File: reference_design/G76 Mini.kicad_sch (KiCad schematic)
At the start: 28 parts, among them J1 Conn_02x16_Odd_Even, J2 JTAG, J3 DB15_Female_HighDensity, U1 EPM240T100, U2 CY7C1018DV33-10VXI, X1 50MHz

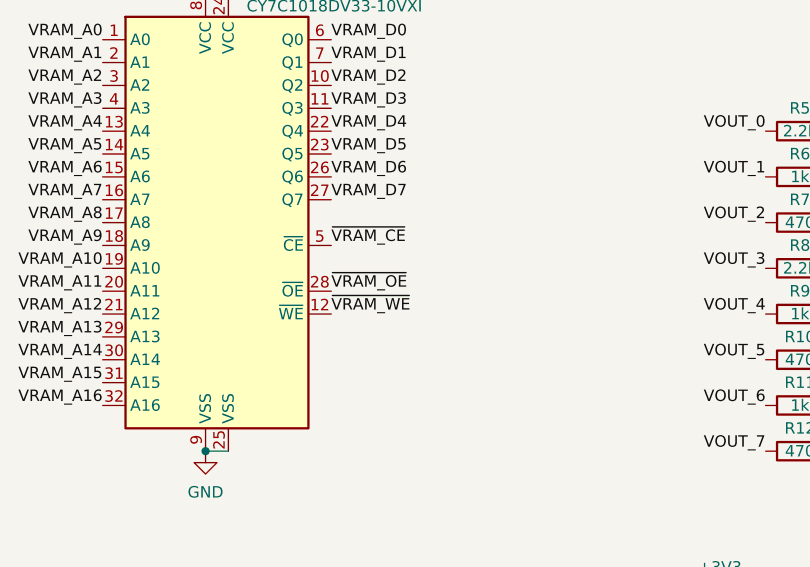
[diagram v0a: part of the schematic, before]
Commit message: Fix CE line on RAM
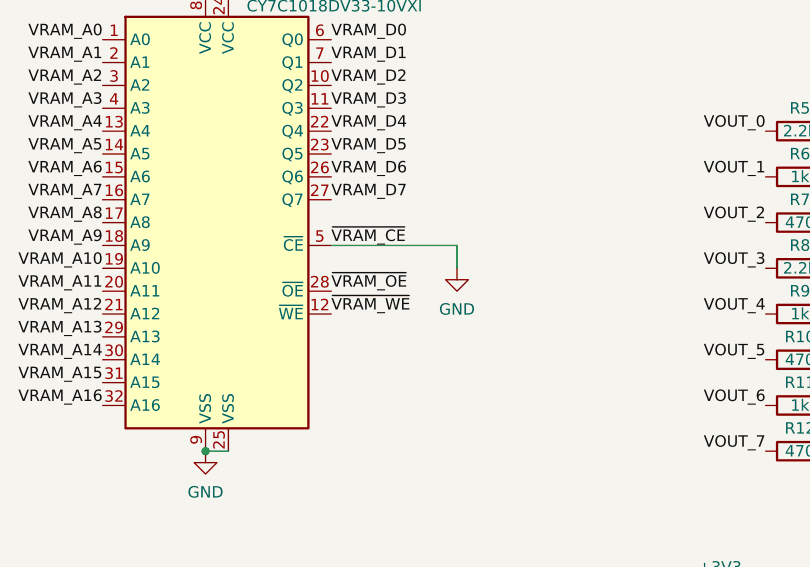
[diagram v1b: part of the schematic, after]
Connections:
- net ~{VRAM_CE} is gone; now on net GND: U2.5 (~{CE})
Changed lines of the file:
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@@
+    (stroke (width 0) (type default) (color 0 0 0 0))
+  )
+  (wire (pts (xy 187.96 95.25) (xy 187.96 97.79))
     (stroke (width 0) (type default) (color 0 0 0 0))
   )
@@
   )
   (wire (pts (xy 217.17 138.43) (xy 219.71 138.43))
+    (stroke (width 0) (type default) (color 0 0 0 0))
+  )
+  (wire (pts (xy 173.99 95.25) (xy 187.96 95.25))
     (stroke (width 0) (type default) (color 0 0 0 0))
   )
@@
     (pin "1")
   )
+  (symbol (lib_id "power:GND") (at 187.96 97.79 0) (unit 1)
+    (in_bom yes) (on_board yes) (fields_autoplaced)
+    (property "Reference" "#PWR?" (id 0) (at 187.96 104.14 0)
+      (effects (font (size 1.27 1.27)) hide)
+    )
+    (property "Value" "GND" (id 1) (at 187.96 102.3525 0))
+    (property "Footprint" "" (id 2) (at 187.96 97.79 0)
+      (effects (font (size 1.27 1.27)) hide)
+    )
+    (property "Datasheet" "" (id 3) (at 187.96 97.79 0)
+      (effects (font (size 1.27 1.27)) hide)
+    )
+    (pin "1")
+  )
   (symbol (lib_id "power:+3V3") (at 217.17 134.62 0) (unit 1)
     (in_bom yes) (on_board yes) (fields_autoplaced)
@@
       (reference "#PWR017") (unit 1) (value "GND") (footprint "")
     )
+    (path "/7bbb7f25-7626-44c0-b756-aa92268a9592"
+      (reference "#PWR?") (unit 1) (value "GND") (footprint "")
+    )
     (path "/b299e2b8-4e0e-4cd0-9ee1-da14b2457e8f"
